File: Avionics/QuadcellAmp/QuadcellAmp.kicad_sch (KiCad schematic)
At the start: 38 parts, among them J1 Screw_Terminal_01x02, U2 LM324N

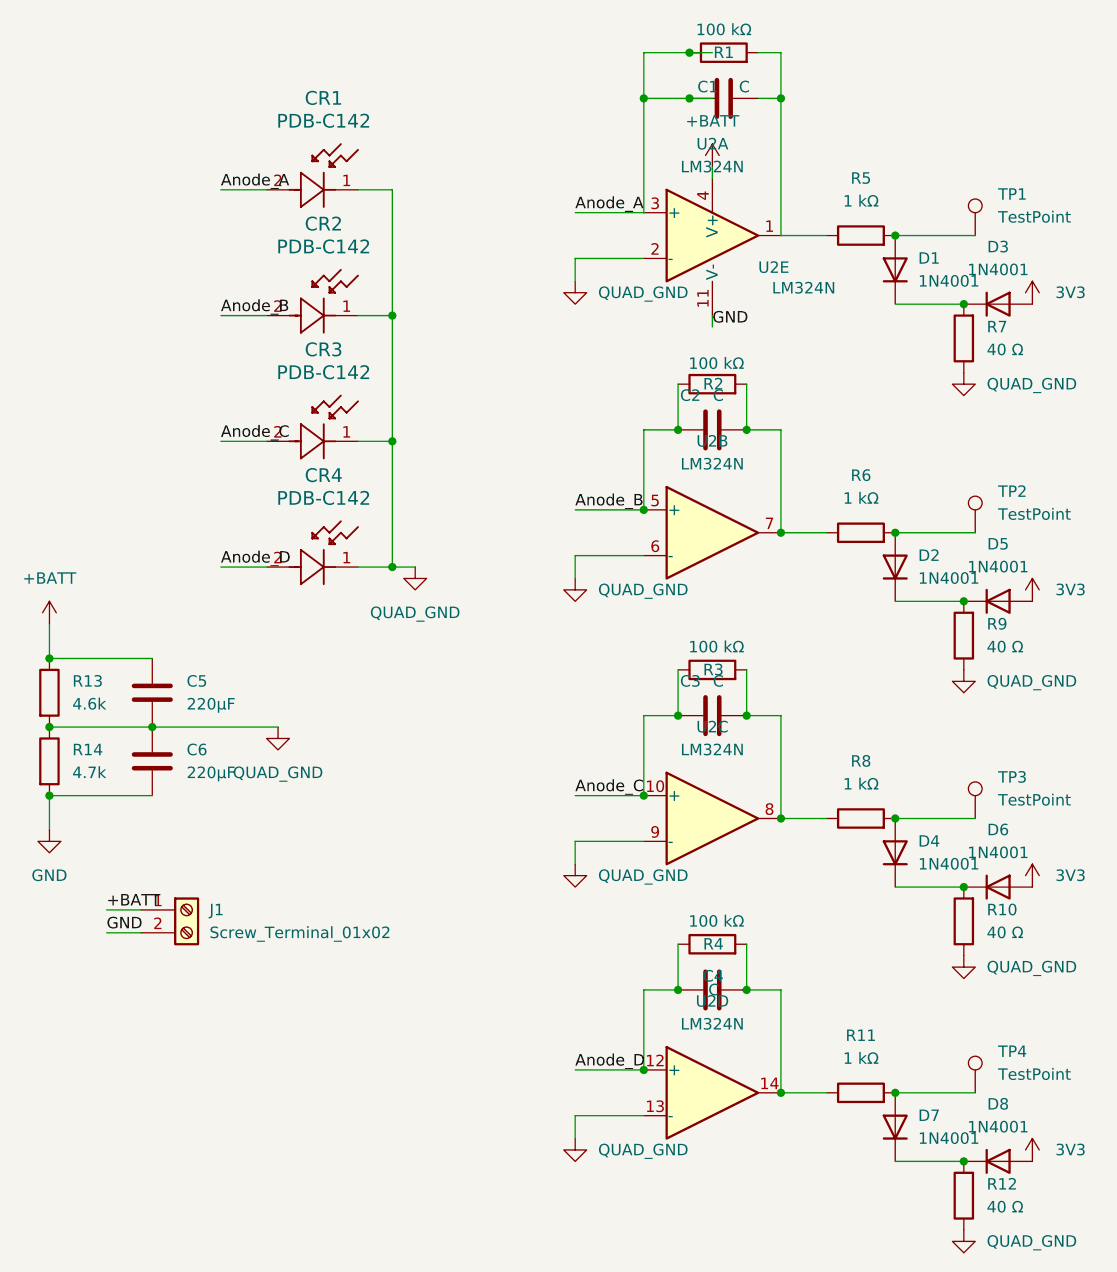
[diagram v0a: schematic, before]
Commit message: Quadcell PD 2.0 finished
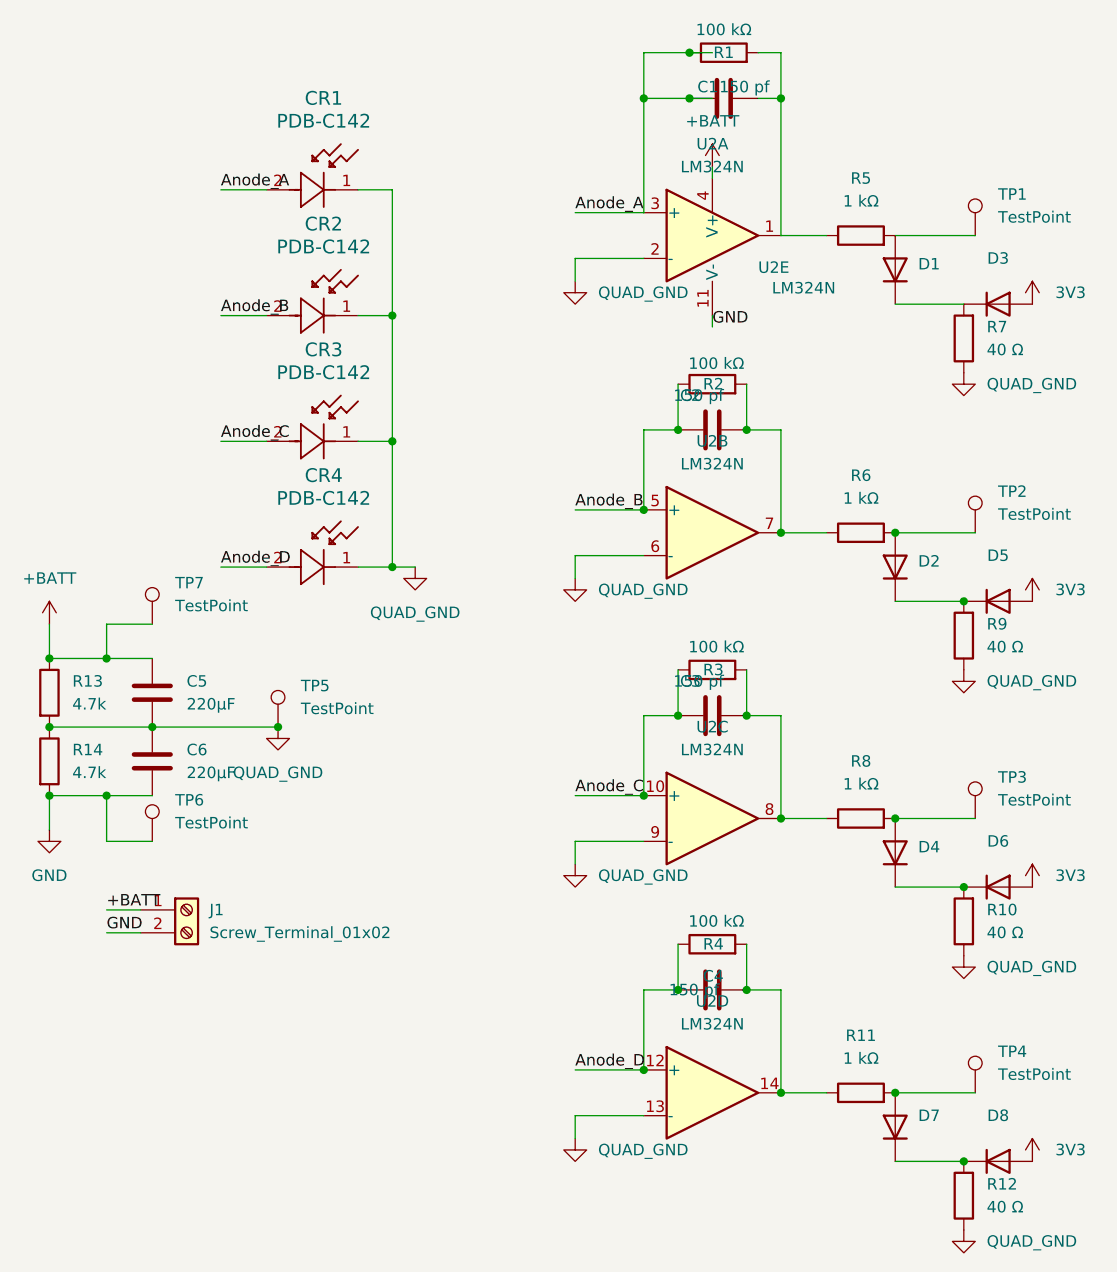
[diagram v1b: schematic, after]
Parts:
- added TP5, TP6, TP7: TestPoint, TestPoint:TestPoint_THTPad_1.0x1.0mm_Drill0.5mm, symbol Connector:TestPoint
- C1, C2, C3, C4: value C -> 150 pf; footprint Capacitor_THT:CP_Axial_L10.0mm_D4.5mm_P15.00mm_Horizontal -> Capacitor_THT:C_Disc_D5.0mm_W2.5mm_P2.50mm
- C5, C6: footprint (none) -> Capacitor_THT:CP_Radial_D5.0mm_P2.00mm
- D1, D2, D3, D4, D5, D6, D7, D8: value 1N4001 -> ~; footprint Diode_THT:D_DO-41_SOD81_P10.16mm_Horizontal -> Diode_THT:D_DO-35_SOD27_P5.08mm_Vertical_AnodeUp
- R1, R10, R11, R12, R14, R2, R3, R4, R5, R6, R7, R8, R9: footprint Resistor_THT:R_Axial_DIN0204_L3.6mm_D1.6mm_P1.90mm_Vertical -> Resistor_THT:R_Axial_DIN0204_L3.6mm_D1.6mm_P2.54mm_Vertical
- R13: value 4.6k -> 4.7k; footprint Resistor_THT:R_Axial_DIN0204_L3.6mm_D1.6mm_P1.90mm_Vertical -> Resistor_THT:R_Axial_DIN0204_L3.6mm_D1.6mm_P2.54mm_Vertical
- TP1, TP2, TP3, TP4: footprint (none) -> TestPoint:TestPoint_THTPad_1.0x1.0mm_Drill0.5mm
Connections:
- net +BATT: now also TP7.1
- net GND: now also TP6.1
- net QUAD_GND: now also TP5.1

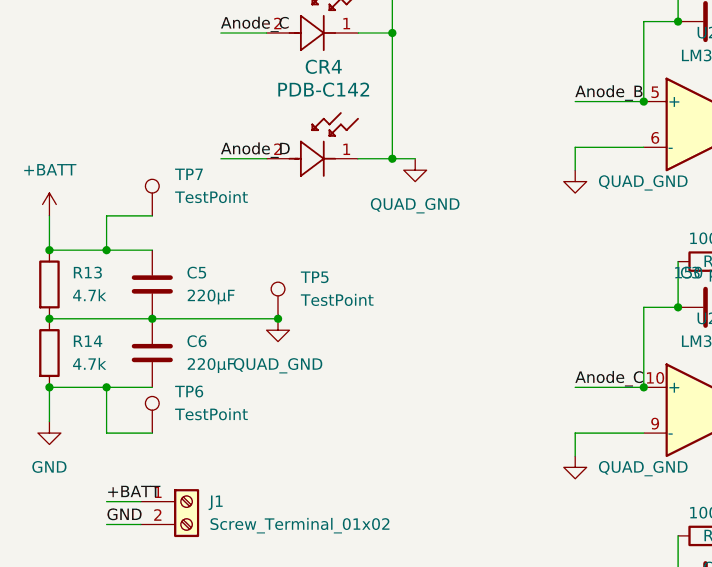
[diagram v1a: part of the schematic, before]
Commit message: added USA flags to pulse footprint library
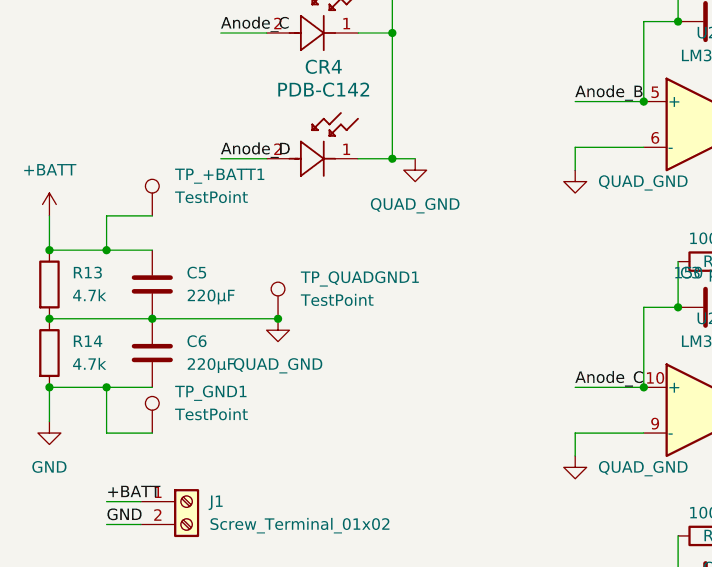
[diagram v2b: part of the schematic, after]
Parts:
- J1: footprint TerminalBlock:TerminalBlock_Xinya_XY308-2.54-2P_1x02_P2.54mm_Horizontal -> TerminalBlock:TerminalBlock_bornier-2_P5.08mm
- renumbered TP7 to TP_+BATT1, TP6 to TP_GND1, TP5 to TP_QUADGND1
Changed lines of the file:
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@@
 		(dnp no)
 		(fields_autoplaced yes)
-		(property "Reference" "TP6"
+		(property "Reference" "TP_GND1"
 			(at 60.96 109.7279 0)
 			(effects
@@
 			(project "QuadcellAmp"
 				(path "/d8c20cce-c8a2-4904-b91b-d44f3cad343b"
-					(reference "TP6")
+					(reference "TP_GND1")
 					(unit 1)
 				)
@@
 		(dnp no)
 		(fields_autoplaced yes)
-		(property "Reference" "TP7"
+		(property "Reference" "TP_+BATT1"
 			(at 60.96 85.5979 0)
 			(effects
@@
 			(project "QuadcellAmp"
 				(path "/d8c20cce-c8a2-4904-b91b-d44f3cad343b"
-					(reference "TP7")
+					(reference "TP_+BATT1")
 					(unit 1)
 				)
@@
 			)
 		)
-		(property "Footprint" "TerminalBlock:TerminalBlock_Xinya_XY308-2.54-2P_1x02_P2.54mm_Horizontal"
+		(property "Footprint" "TerminalBlock:TerminalBlock_bornier-2_P5.08mm"
 			(at 62.23 121.92 0)
 			(effects
@@
 		(dnp no)
 		(fields_autoplaced yes)
-		(property "Reference" "TP5"
+		(property "Reference" "TP_QUADGND1"
 			(at 74.93 97.0279 0)
 			(effects
@@
 			(project "QuadcellAmp"
 				(path "/d8c20cce-c8a2-4904-b91b-d44f3cad343b"
-					(reference "TP5")
-					(unit 1)
-				)
+					(reference "TP_QUADGND1")
+					(unit 1)
+				)

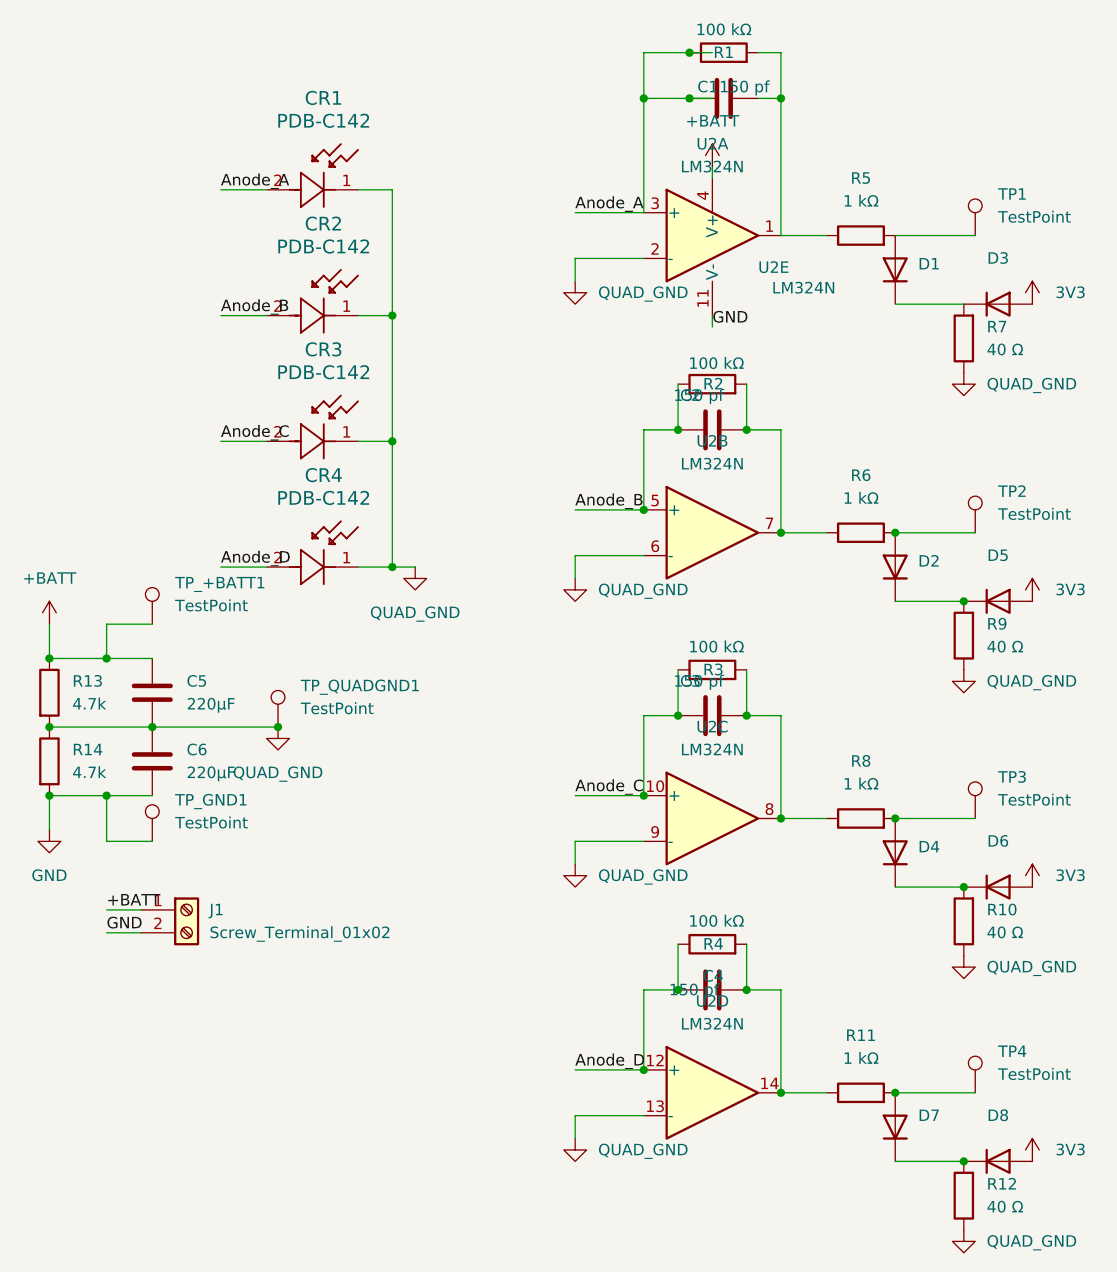
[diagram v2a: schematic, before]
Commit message: flipped op amp signs :/
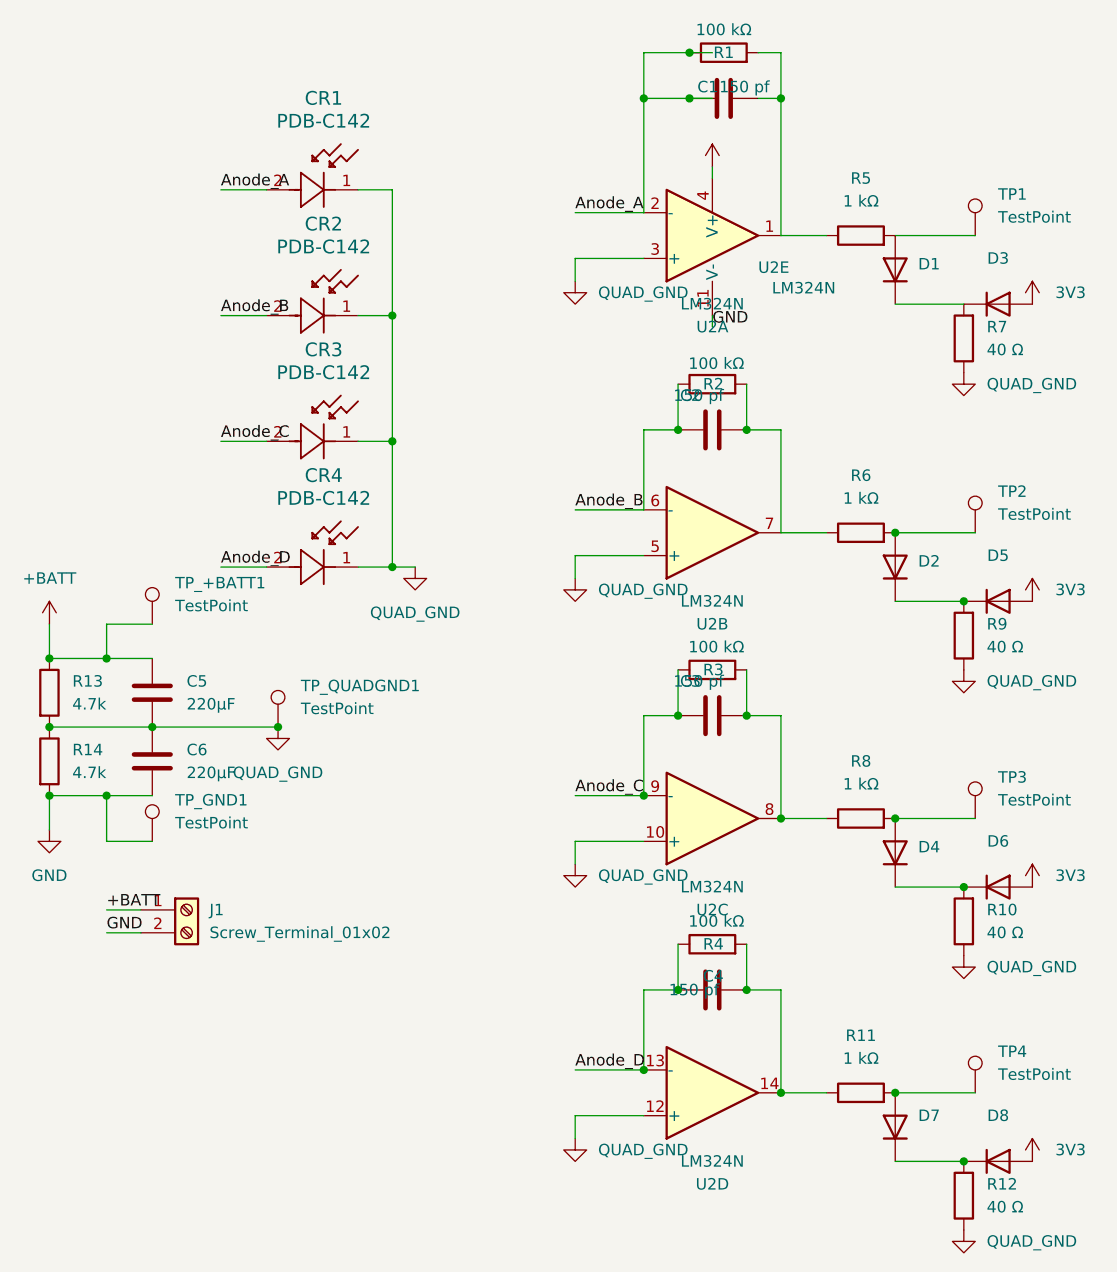
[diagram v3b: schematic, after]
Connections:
- net Anode_A: now also U2.2 (-); no longer U2.3 (+)
- net Anode_B: now also U2.6 (-); no longer U2.5 (+)
- net Anode_C: now also U2.9 (-); no longer U2.10 (+)
- net Anode_D: now also U2.13 (-); no longer U2.12 (+)
- net QUAD_GND: now also U2.10 (+), U2.12 (+), U2.3 (+), U2.5 (+); no longer U2.13 (-), U2.2 (-), U2.6 (-), U2.9 (-)
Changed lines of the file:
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@@
 	)
 	(junction
-		(at 113.03 77.47)
-		(diameter 0)
-		(color 0 0 0 0)
-	)
-	(junction
 		(at 53.34 93.98)
 		(diameter 0)
@@
 	)
 	(junction
-		(at 128.27 80.01)
-		(diameter 0)
-		(color 0 0 0 0)
-	)
-	(junction
 		(at 148.59 119.38)
 		(diameter 0)
@@
 	(wire
 		(pts
-			(xy 128.27 46.99) (xy 128.27 31.75)
+			(xy 128.27 31.75) (xy 128.27 46.99)
 		)
 		(stroke
@@
 					(size 1.27 1.27)
 				)
+				(hide yes)
 			)
 		)
@@
 		(lib_id "Amplifier_Operational:OPA1679")
 		(at 120.65 46.99 0)
+		(mirror x)
 		(unit 1)
 		(exclude_from_sim no)
@@
 		(on_board yes)
 		(dnp no)
-		(fields_autoplaced yes)
 		(property "Reference" "U2"
-			(at 120.65 36.83 0)
+			(at 120.65 57.15 0)
 			(effects
 				(font
@@
 		)
 		(property "Value" "LM324N"
-			(at 120.65 39.37 0)
+			(at 120.65 54.61 0)
 			(effects
 				(font
@@
 		)
 		(property "Footprint" "LM324:N14"
-			(at 119.38 44.45 0)
+			(at 119.38 49.53 0)
 			(effects
 				(font
@@
 		)
 		(property "Datasheet" "http://www.ti.com/lit/ds/symlink/opa1678.pdf"
-			(at 121.92 41.91 0)
+			(at 121.92 52.07 0)
 			(effects
 				(font
@@
 		(lib_id "Amplifier_Operational:OPA1679")
 		(at 120.65 80.01 0)
+		(mirror x)
 		(unit 2)
 		(exclude_from_sim no)
@@
 		(fields_autoplaced yes)
 		(property "Reference" "U2"
-			(at 120.65 69.85 0)
+			(at 120.65 90.17 0)
 			(effects
 				(font
@@
 		)
 		(property "Value" "LM324N"
-			(at 120.65 72.39 0)
+			(at 120.65 87.63 0)
 			(effects
 				(font
@@
 		)
 		(property "Footprint" "LM324:N14"
-			(at 119.38 77.47 0)
+			(at 119.38 82.55 0)
 			(effects
 				(font
@@
 		)
 		(property "Datasheet" "http://www.ti.com/lit/ds/symlink/opa1678.pdf"
-			(at 121.92 74.93 0)
+			(at 121.92 85.09 0)
 			(effects
 				(font
@@
 		(lib_id "Amplifier_Operational:OPA1679")
 		(at 120.65 111.76 0)
+		(mirror x)
 		(unit 3)
 		(exclude_from_sim no)
@@
 		(fields_autoplaced yes)
 		(property "Reference" "U2"
-			(at 120.65 101.6 0)
+			(at 120.65 121.92 0)
 			(effects
 				(font
@@
 		)
 		(property "Value" "LM324N"
-			(at 120.65 104.14 0)
+			(at 120.65 119.38 0)
 			(effects
 				(font
@@
 		)
 		(property "Footprint" "LM324:N14"
-			(at 119.38 109.22 0)
+			(at 119.38 114.3 0)
 			(effects
 				(font
@@
 		)
 		(property "Datasheet" "http://www.ti.com/lit/ds/symlink/opa1678.pdf"
-			(at 121.92 106.68 0)
+			(at 121.92 116.84 0)
 			(effects
 				(font
@@
 		(lib_id "Amplifier_Operational:OPA1679")
 		(at 120.65 142.24 0)
+		(mirror x)
 		(unit 4)
 		(exclude_from_sim no)
@@
 		(fields_autoplaced yes)
 		(property "Reference" "U2"
-			(at 120.65 132.08 0)
+			(at 120.65 152.4 0)
 			(effects
 				(font
@@
 		)
 		(property "Value" "LM324N"
-			(at 120.65 134.62 0)
+			(at 120.65 149.86 0)
 			(effects
 				(font
@@
 		)
 		(property "Footprint" "LM324:N14"
-			(at 119.38 139.7 0)
+			(at 119.38 144.78 0)
 			(effects
 				(font
@@
 		)
 		(property "Datasheet" "http://www.ti.com/lit/ds/symlink/opa1678.pdf"
-			(at 121.92 137.16 0)
+			(at 121.92 147.32 0)
 			(effects
 				(font
